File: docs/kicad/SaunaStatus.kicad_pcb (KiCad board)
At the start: 2 copper layers, 153 x 101 mm, 14 parts, among them J1 Adafruit-MAX31865-Breakout, J2 28BYJ-48, J3 28BYJ-48, J4 DHT21/AM2301 Ceiling, J5 DHT21/AM2301 Bench, U1 ESP32-DevKit-V1-DOIT

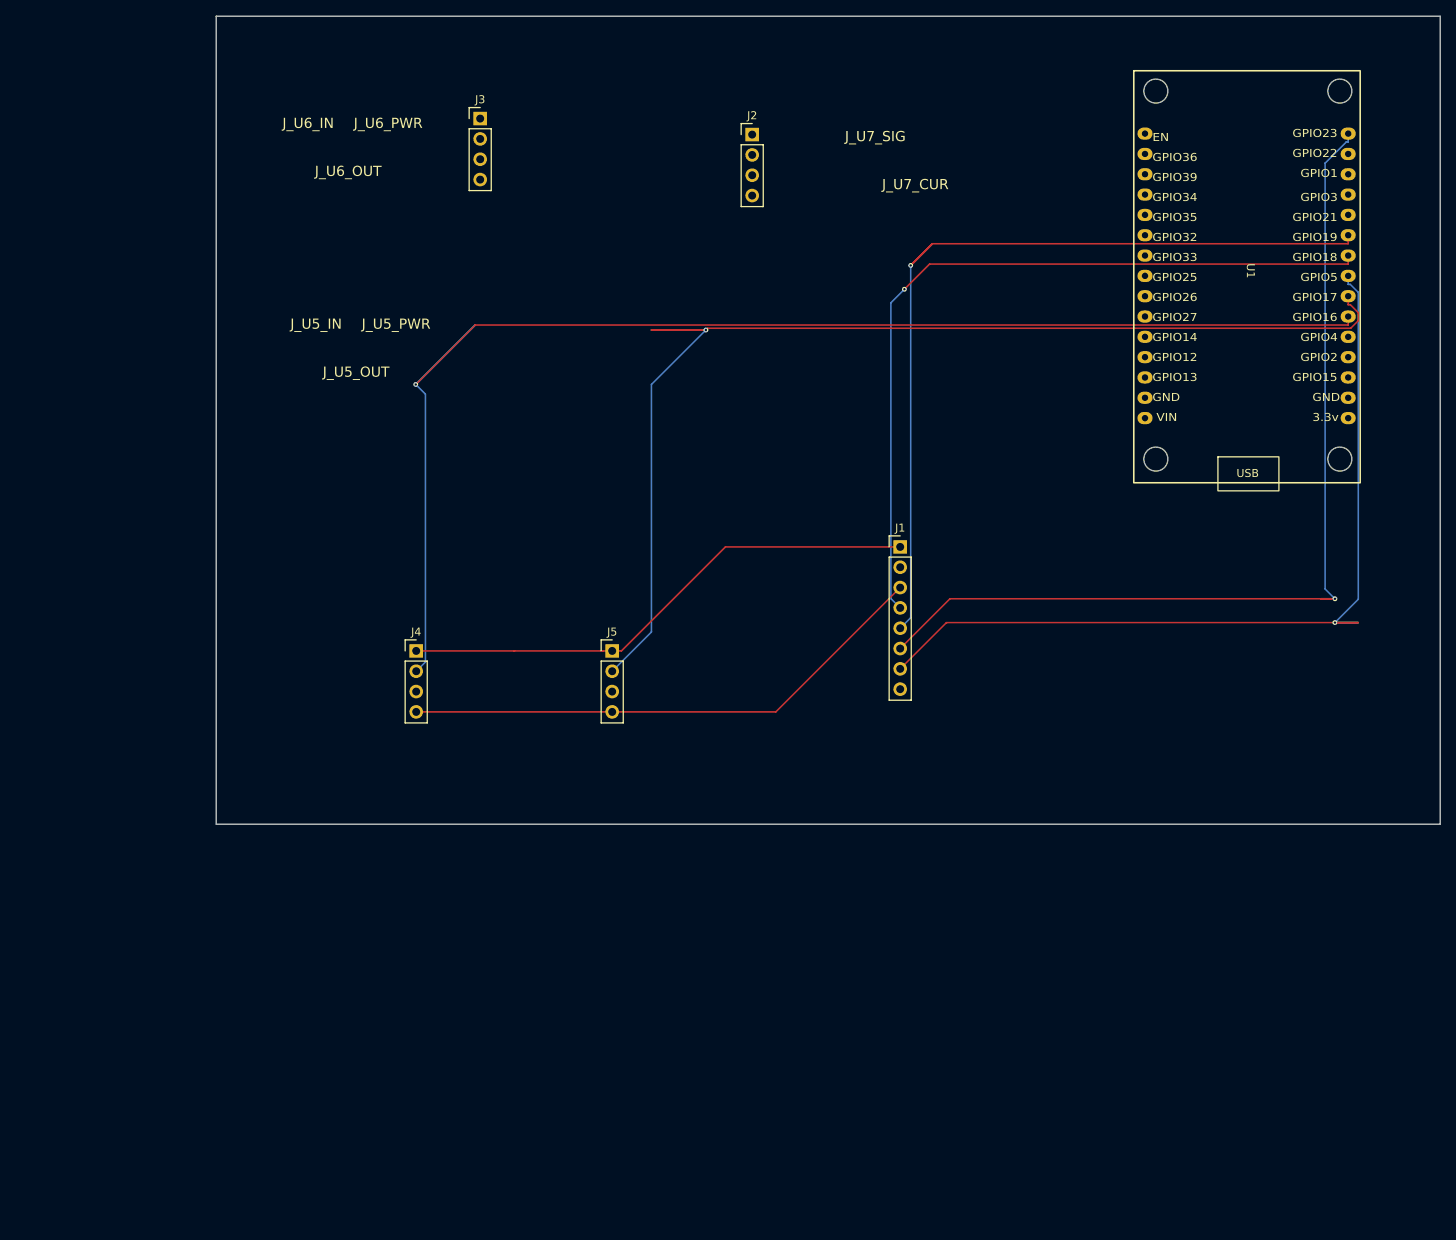
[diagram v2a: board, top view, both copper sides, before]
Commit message: fix(kicad): resolve schematic/PCB parity to unblock pcb import
Root cause: the kicad_sch root scope was prematurely closed by a spurious
')' at line 3626, placing J_LEFT, J_RIGHT, J1–J5 and all connector stubs
outside the (kicad_sch) scope. KiCad's netlist exporter and ERC engine
ignored everything after that line, causing 126 ERC violations and a crash
on pcb import.

Schematic fixes:
- Remove spurious ')' that exited the root (kicad_sch) scope at line 3626
- Add Footprint properties to J_LEFT, J_RIGHT, J_U5_IN/OUT/PWR,
  J_U6_IN/OUT/PWR, J_U7_SIG/CUR (was empty, caused footprint_symbol_mismatch)

PCB fixes:
- Add J_LEFT / J_RIGHT (PinHeader_1x20) footprints with all 20 pads each;
  net assignments per schematic (OUTFLOW_I1-I4, INFLOW_I1-I4, SPI/I2C, etc.)
- Add pad definitions to connector stubs (J_U5_IN, J_U5_OUT, J_U5_PWR,
  J_U6_IN, J_U6_OUT, J_U6_PWR, J_U7_SIG, J_U7_CUR) — stubs had footprint
  shells but no pads, causing net_conflict in parity check
- Update component values to match schematic (e.g. "ULN2003A-IN" →
  "ULN2003A-Input-Outflow", "INA260-JP2" → "Adafruit-INA260-JP2", etc.)
- Add 36 new nets to global net table: +5V, /INA_IN+, and 34 unconnected-*
  nets for no_connect pins on J_LEFT, J_RIGHT, and connector stubs

Result:
- kicad-cli sch erc: 0 errors (86 warnings, non-blocking)
- kicad-cli pcb drc --schematic-parity: 0 blocking parity violations
- pcb import: exit 0; SaunaStatus.zen written
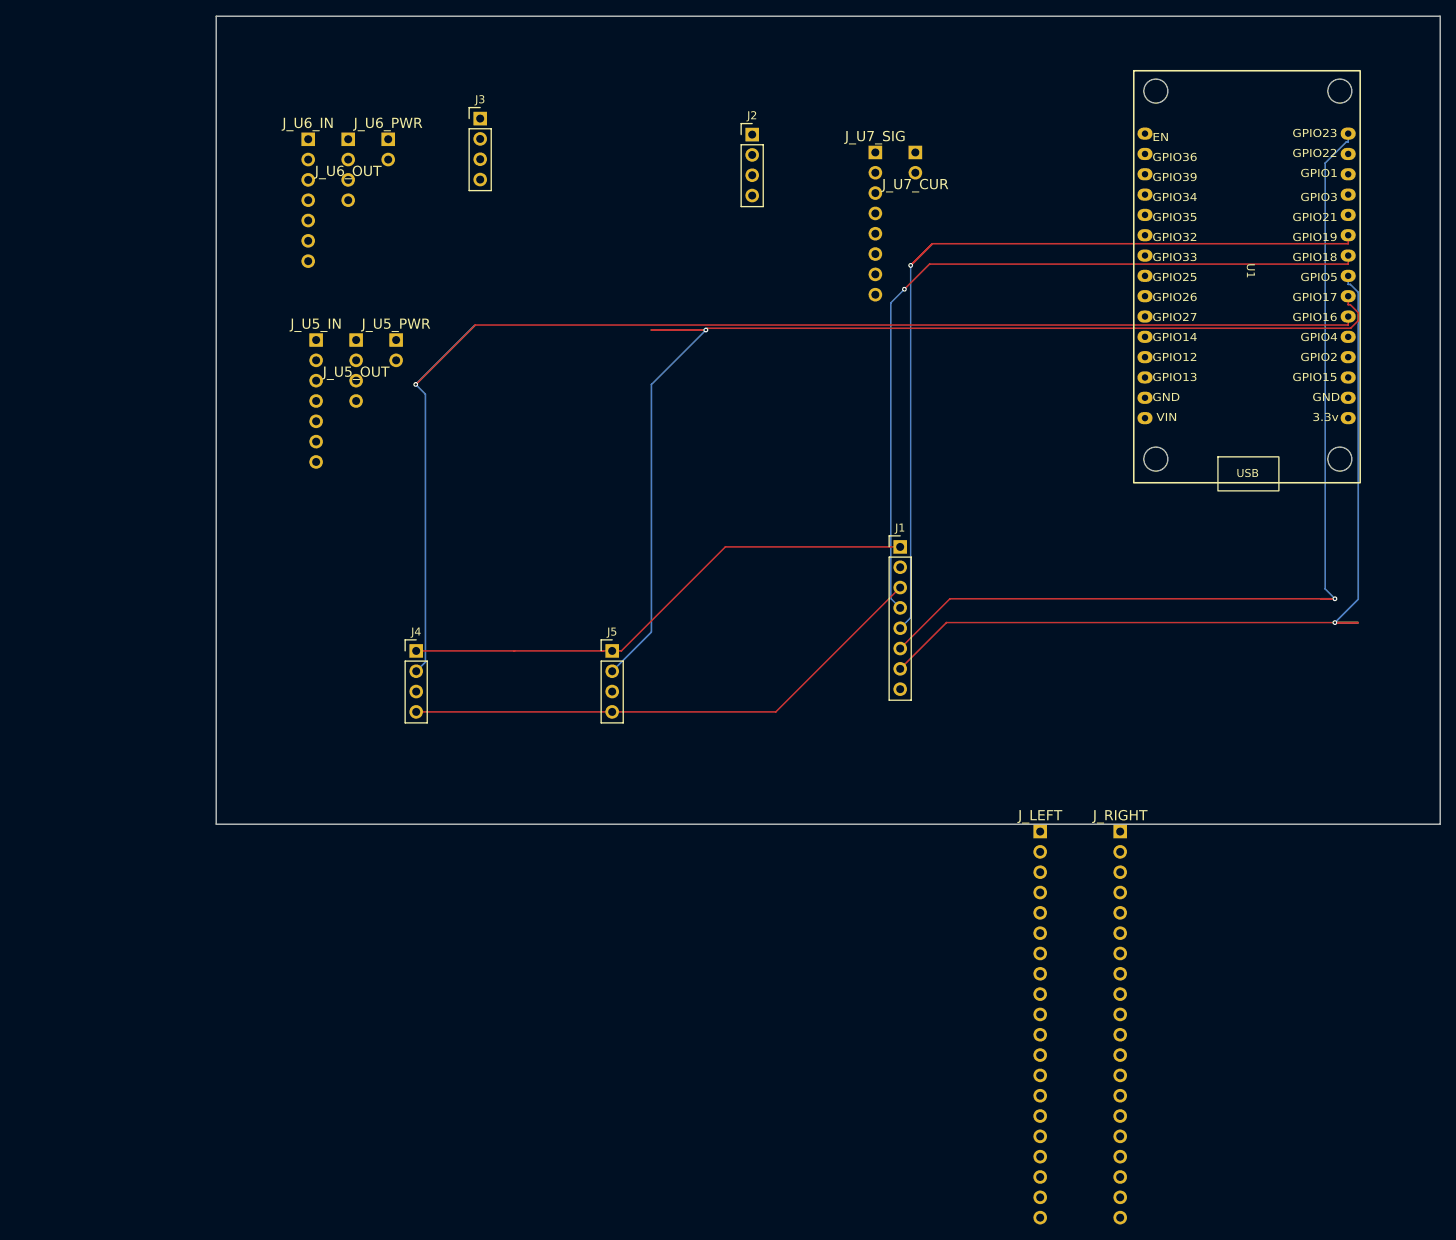
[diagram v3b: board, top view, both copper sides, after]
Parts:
- added J_LEFT: LB-ESP32S3-Left-Header, Connector_PinHeader_2.54mm:PinHeader_1x20_P2.54mm_Vertical, F.Cu at (195.0, 120.0)
- added J_RIGHT: LB-ESP32S3-Right-Header, Connector_PinHeader_2.54mm:PinHeader_1x20_P2.54mm_Vertical, F.Cu at (205.0, 120.0)
- J_U5_IN: value ULN2003A-IN -> ULN2003A-Input-Outflow
- J_U5_OUT: value ULN2003A-OUT -> 28BYJ-48-Outflow
- J_U5_PWR: value ULN2003A-PWR -> ULN2003A-Power-Outflow
- J_U6_IN: value ULN2003A-IN -> ULN2003A-Input-Inflow
- J_U6_OUT: value ULN2003A-OUT -> 28BYJ-48-Inflow
- J_U6_PWR: value ULN2003A-PWR -> ULN2003A-Power-Inflow
- J_U7_CUR: value INA260-X1 -> Adafruit-INA260-X1
- J_U7_SIG: value INA260-JP2 -> Adafruit-INA260-JP2
